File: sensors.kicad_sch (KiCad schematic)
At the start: 28 parts, among them J10 Conn_Coaxial, U3 LSM6DSOXTR, U4 LIS3MDL, U5 BNO055, U6 BME280, U7 ATGM336H-5N31, Y3 32.768KHz 12.5pF

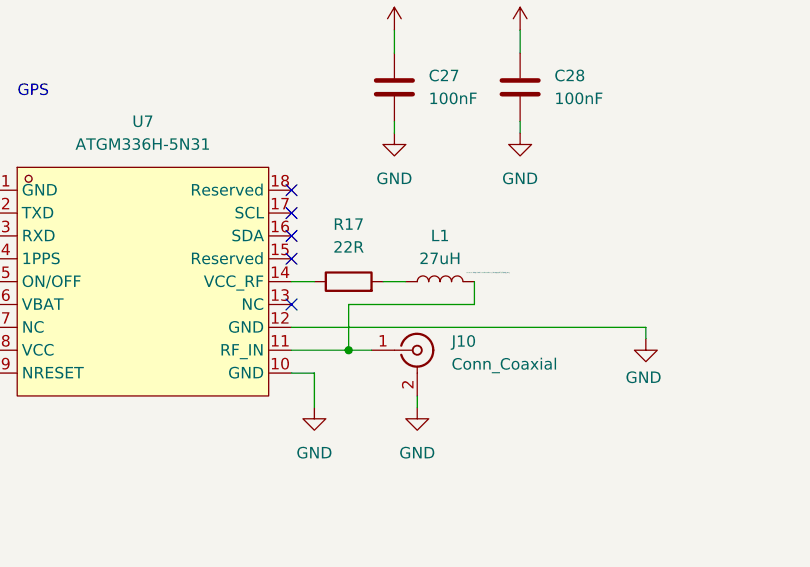
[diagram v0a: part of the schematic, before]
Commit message: GPS Bias tee upgrade
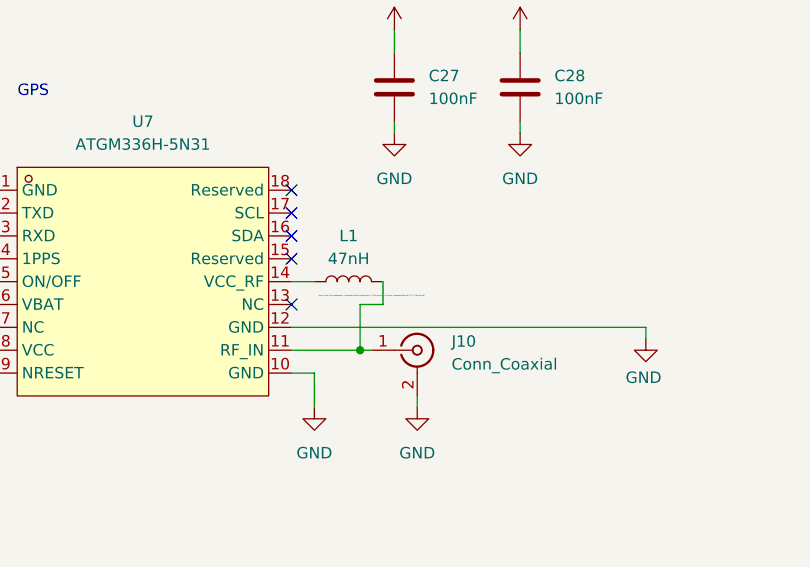
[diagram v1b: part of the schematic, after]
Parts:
- removed R17: 22R, symbol Device:R
- L1: value 27uH -> 47nH
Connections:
- net at U7.14 (VCC_RF): now also L1.1
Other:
- note added: "source: http://wiki.sunfounder.cc/images/f/f1/Gsdg.png and page 13 of https://www.tinytronics.nl/product_files/002176_ATGM336H.pdf"
- note removed: "source: http://wiki.sunfounder.cc/images/f/f1/Gsdg.png"
- moved on the sheet: L1
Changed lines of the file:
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@@
 		)
 	)
-	(text "source: http://wiki.sunfounder.cc/images/f/f1/Gsdg.png"
+	(text "source: http://wiki.sunfounder.cc/images/f/f1/Gsdg.png and page 13 of https://www.tinytronics.nl/product_files/002176_ATGM336H.pdf"
 		(exclude_from_sim no)
-		(at 171.704 149.098 0)
+		(at 158.75 151.638 0)
 		(effects
 			(font
@@
 	)
 	(junction
-		(at 156.21 157.48)
-		(diameter 0)
-		(color 0 0 0 0)
-	)
-	(junction
 		(at 175.26 52.07)
 		(diameter 0)
@@
 		(color 0 0 0 0)
 	)
+	(junction
+		(at 157.48 157.48)
+		(diameter 0)
+		(color 0 0 0 0)
+	)
 	(no_connect
 		(at 116.84 154.94)
@@
 	(wire
 		(pts
-			(xy 170.18 149.86) (xy 170.18 152.4)
+			(xy 157.48 152.4) (xy 157.48 157.48)
 		)
 		(stroke
@@
 	(wire
 		(pts
-			(xy 160.02 149.86) (xy 162.56 149.86)
+			(xy 114.3 157.48) (xy 116.84 157.48)
 		)
 		(stroke
@@
 	(wire
 		(pts
-			(xy 114.3 157.48) (xy 116.84 157.48)
+			(xy 53.34 66.04) (xy 67.31 66.04)
 		)
 		(stroke
@@
 	(wire
 		(pts
-			(xy 53.34 66.04) (xy 67.31 66.04)
+			(xy 91.44 158.75) (xy 113.03 158.75)
 		)
 		(stroke
@@
 	(wire
 		(pts
-			(xy 91.44 158.75) (xy 113.03 158.75)
+			(xy 152.4 149.86) (xy 149.86 149.86)
 		)
 		(stroke
@@
 	(wire
 		(pts
-			(xy 156.21 157.48) (xy 158.75 157.48)
-		)
-		(stroke
-			(width 0)
-			(type default)
-		)
-	)
-	(wire
-		(pts
 			(xy 95.25 140.97) (xy 95.25 138.43)
 		)
@@
 	(wire
 		(pts
-			(xy 189.23 156.21) (xy 189.23 154.94)
+			(xy 160.02 152.4) (xy 160.02 149.86)
 		)
 		(stroke
@@
 	(wire
 		(pts
-			(xy 99.06 91.44) (xy 99.06 93.98)
+			(xy 189.23 156.21) (xy 189.23 154.94)
 		)
 		(stroke
@@
 	(wire
 		(pts
-			(xy 181.61 46.99) (xy 175.26 46.99)
+			(xy 99.06 91.44) (xy 99.06 93.98)
 		)
 		(stroke
@@
 	(wire
 		(pts
-			(xy 233.68 39.37) (xy 233.68 36.83)
+			(xy 181.61 46.99) (xy 175.26 46.99)
 		)
 		(stroke
@@
 	(wire
 		(pts
-			(xy 257.81 92.71) (xy 260.35 92.71)
+			(xy 233.68 39.37) (xy 233.68 36.83)
 		)
 		(stroke
@@
 	(wire
 		(pts
-			(xy 170.18 152.4) (xy 156.21 152.4)
+			(xy 257.81 92.71) (xy 260.35 92.71)
 		)
 		(stroke
@@
 	(wire
 		(pts
-			(xy 156.21 152.4) (xy 156.21 157.48)
-		)
-		(stroke
-			(width 0)
-			(type default)
-		)
-	)
-	(wire
-		(pts
 			(xy 101.6 143.51) (xy 101.6 140.97)
 		)
@@
 	(wire
 		(pts
-			(xy 149.86 157.48) (xy 156.21 157.48)
+			(xy 149.86 157.48) (xy 157.48 157.48)
 		)
 		(stroke
@@
 	(wire
 		(pts
+			(xy 157.48 157.48) (xy 158.75 157.48)
+		)
+		(stroke
+			(width 0)
+			(type default)
+		)
+	)
+	(wire
+		(pts
 			(xy 100.33 81.28) (xy 110.49 81.28)
 		)
@@
 	(wire
 		(pts
+			(xy 157.48 152.4) (xy 160.02 152.4)
+		)
+		(stroke
+			(width 0)
+			(type default)
+		)
+	)
+	(wire
+		(pts
 			(xy 116.84 83.82) (xy 111.76 83.82)
 		)
@@
 	(wire
 		(pts
-			(xy 149.86 149.86) (xy 152.4 149.86)
-		)
-		(stroke
-			(width 0)
-			(type default)
-		)
-	)
-	(wire
-		(pts
 			(xy 102.87 147.32) (xy 102.87 143.51)
 		)
@@
 	)
 	(symbol
-		(lib_id "Device:R")
-		(at 156.21 149.86 90)
-		(unit 1)
-		(exclude_from_sim no)
-		(in_bom yes)
-		(on_board yes)
-		(dnp no)
-		(fields_autoplaced yes)
-		(property "Reference" "R17"
-			(at 156.21 143.51 90)
-			(effects
-				(font
-					(size 1.27 1.27)
-				)
-			)
-		)
-		(property "Value" "22R"
-			(at 156.21 146.05 90)
-			(effects
-				(font
-					(size 1.27 1.27)
-				)
-			)
-		)
-		(property "Footprint" ""
-			(at 156.21 151.638 90)
-			(effects
-				(font
-					(size 1.27 1.27)
-				)
-				(hide yes)
-			)
-		)
-		(property "Datasheet" "~"
-			(at 156.21 149.86 0)
-			(effects
-				(font
-					(size 1.27 1.27)
-				)
-				(hide yes)
-			)
-		)
-		(property "Description" "Resistor"
-			(at 156.21 149.86 0)
-			(effects
-				(font
-					(size 1.27 1.27)
-				)
-				(hide yes)
-			)
-		)
-		(pin "1"
-		)
-		(pin "2"
-		)
-		(instances
-			(project ""
-				(path "/e99ca14d-cacc-4390-92ee-6dcff8e13ef3/ec279230-54a0-4e30-9b23-a4126e2291f2"
-					(reference "R17")
-					(unit 1)
-				)
-			)
-		)
-	)
-	(symbol
 		(lib_id "Device:C")
 		(at 111.76 54.61 90)
@@
 	(symbol
 		(lib_id "Device:L")
-		(at 166.37 149.86 90)
+		(at 156.21 149.86 90)
 		(unit 1)
 		(exclude_from_sim no)
@@
 		(on_board yes)
 		(dnp no)
-		(fields_autoplaced yes)
 		(property "Reference" "L1"
-			(at 166.37 144.78 90)
+			(at 156.21 144.78 90)
 			(effects
 				(font
@@
 			)
 		)
-		(property "Value" "27uH"
-			(at 166.37 147.32 90)
+		(property "Value" "47nH"
+			(at 156.21 147.32 90)
 			(effects
 				(font
@@
 		)
 		(property "Footprint" ""
-			(at 166.37 149.86 0)
+			(at 156.21 149.86 0)
 			(effects
 				(font
@@
 		)
 		(property "Datasheet" "~"
-			(at 166.37 149.86 0)
+			(at 156.21 149.86 0)
 			(effects
 				(font
@@
 		)
 		(property "Description" "Inductor"
-			(at 166.37 149.86 0)
+			(at 156.21 149.86 0)
 			(effects
 				(font

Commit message: Add more footprints!
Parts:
- C10, C11, C12, C13: footprint (none) -> Capacitor_SMD:C_0402_1005Metric_Pad0.74x0.62mm_HandSolder
- C14, C27, C28, C8, C9: footprint Capacitor_SMD:C_0603_1608Metric_Pad1.08x0.95mm_HandSolder -> Capacitor_SMD:C_0402_1005Metric_Pad0.74x0.62mm_HandSolder
- L1: footprint (none) -> Inductor_SMD:L_0603_1608Metric_Pad1.05x0.95mm_HandSolder
- R1, R19, R2, R3, R4, R7: footprint (none) -> Resistor_SMD:R_0402_1005Metric_Pad0.72x0.64mm_HandSolder
- R16, R18, R9: footprint Resistor_SMD:R_0603_1608Metric_Pad0.98x0.95mm_HandSolder -> Resistor_SMD:R_0402_1005Metric_Pad0.72x0.64mm_HandSolder
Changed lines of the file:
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@@
 			)
 		)
-		(property "Footprint" "Resistor_SMD:R_0603_1608Metric_Pad0.98x0.95mm_HandSolder"
+		(property "Footprint" "Resistor_SMD:R_0402_1005Metric_Pad0.72x0.64mm_HandSolder"
 			(at 59.69 164.592 90)
 			(effects
@@
 			)
 		)
-		(property "Footprint" ""
+		(property "Footprint" "Capacitor_SMD:C_0402_1005Metric_Pad0.74x0.62mm_HandSolder"
 			(at 257.81 91.7448 0)
 			(effects
@@
 			)
 		)
-		(property "Footprint" "Resistor_SMD:R_0603_1608Metric_Pad0.98x0.95mm_HandSolder"
+		(property "Footprint" "Resistor_SMD:R_0402_1005Metric_Pad0.72x0.64mm_HandSolder"
 			(at 62.23 152.908 90)
 			(effects
@@
 			)
 		)
-		(property "Footprint" "Capacitor_SMD:C_0603_1608Metric_Pad1.08x0.95mm_HandSolder"
+		(property "Footprint" "Capacitor_SMD:C_0402_1005Metric_Pad0.74x0.62mm_HandSolder"
 			(at 176.2252 132.08 0)
 			(effects
@@
 			)
 		)
-		(property "Footprint" "Capacitor_SMD:C_0603_1608Metric_Pad1.08x0.95mm_HandSolder"
+		(property "Footprint" "Capacitor_SMD:C_0402_1005Metric_Pad0.74x0.62mm_HandSolder"
 			(at 115.57 53.6448 0)
 			(effects
@@
 			)
 		)
-		(property "Footprint" "Capacitor_SMD:C_0603_1608Metric_Pad1.08x0.95mm_HandSolder"
+		(property "Footprint" "Capacitor_SMD:C_0402_1005Metric_Pad0.74x0.62mm_HandSolder"
 			(at 115.57 68.8848 0)
 			(effects
@@
 			)
 		)
-		(property "Footprint" ""
+		(property "Footprint" "Capacitor_SMD:C_0402_1005Metric_Pad0.74x0.62mm_HandSolder"
 			(at 189.23 46.0248 0)
 			(effects
@@
 			)
 		)
-		(property "Footprint" ""
+		(property "Footprint" "Resistor_SMD:R_0402_1005Metric_Pad0.72x0.64mm_HandSolder"
 			(at 231.902 33.02 90)
 			(effects
@@
 			)
 		)
-		(property "Footprint" ""
+		(property "Footprint" "Resistor_SMD:R_0402_1005Metric_Pad0.72x0.64mm_HandSolder"
 			(at 224.282 120.65 90)
 			(effects
@@
 			)
 		)
-		(property "Footprint" "Capacitor_SMD:C_0603_1608Metric_Pad1.08x0.95mm_HandSolder"
+		(property "Footprint" "Capacitor_SMD:C_0402_1005Metric_Pad0.74x0.62mm_HandSolder"
 			(at 162.2552 132.08 0)
 			(effects
@@
 			)
 		)
-		(property "Footprint" ""
+		(property "Footprint" "Capacitor_SMD:C_0402_1005Metric_Pad0.74x0.62mm_HandSolder"
 			(at 265.1252 121.92 0)
 			(effects
@@
 			)
 		)
-		(property "Footprint" ""
+		(property "Footprint" "Resistor_SMD:R_0402_1005Metric_Pad0.72x0.64mm_HandSolder"
 			(at 57.912 86.36 90)
 			(effects
@@
 			)
 		)
-		(property "Footprint" ""
+		(property "Footprint" "Resistor_SMD:R_0402_1005Metric_Pad0.72x0.64mm_HandSolder"
 			(at 60.452 50.8 90)
 			(effects
@@
 			)
 		)
-		(property "Footprint" "Capacitor_SMD:C_0603_1608Metric_Pad1.08x0.95mm_HandSolder"
+		(property "Footprint" "Capacitor_SMD:C_0402_1005Metric_Pad0.74x0.62mm_HandSolder"
 			(at 43.18 141.9352 0)
 			(effects
@@
 			)
 		)
-		(property "Footprint" ""
+		(property "Footprint" "Inductor_SMD:L_0603_1608Metric_Pad1.05x0.95mm_HandSolder"
 			(at 156.21 149.86 0)
 			(effects
@@
 			)
 		)
-		(property "Footprint" ""
+		(property "Footprint" "Capacitor_SMD:C_0402_1005Metric_Pad0.74x0.62mm_HandSolder"
 			(at 100.0252 91.44 0)
 			(effects
@@
 			)
 		)
-		(property "Footprint" ""
+		(property "Footprint" "Resistor_SMD:R_0402_1005Metric_Pad0.72x0.64mm_HandSolder"
 			(at 93.472 124.46 90)
 			(effects
@@
 			)
 		)
-		(property "Footprint" "Resistor_SMD:R_0603_1608Metric_Pad0.98x0.95mm_HandSolder"
+		(property "Footprint" "Resistor_SMD:R_0402_1005Metric_Pad0.72x0.64mm_HandSolder"
 			(at 99.06 151.638 90)
 			(effects
@@
 			)
 		)
-		(property "Footprint" ""
+		(property "Footprint" "Resistor_SMD:R_0402_1005Metric_Pad0.72x0.64mm_HandSolder"
 			(at 221.742 33.02 90)
 			(effects

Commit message: More schematic work
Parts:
- D1: footprint (none) -> LED_SMD:LED_0603_1608Metric
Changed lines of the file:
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@@
 			)
 		)
-		(property "Footprint" ""
+		(property "Footprint" "LED_SMD:LED_0603_1608Metric"
 			(at 95.25 134.62 0)
 			(effects

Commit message: Reset circuit fix (oops...)
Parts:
- removed C27, C28: 100nF, Capacitor_SMD:C_0402_1005Metric_Pad0.74x0.62mm_HandSolder, symbol Device:C
- added C31, C34, C38, C40, C41, C44: 100nF, Capacitor_SMD:C_0402_1005Metric_Pad0.74x0.62mm_HandSolder, symbol Device:C
- added C35, C39, C42, C45: 10uF, Capacitor_SMD:C_0402_1005Metric_Pad0.74x0.62mm_HandSolder, symbol Device:C
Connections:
- net +3.3V: now also C31.1, C34.1, C35.1, C38.1, C39.1, C40.1, C41.1, C42.1, C44.1, C45.1
- net GND: now also C31.2, C34.2, C35.2, C38.2, C39.2, C40.2, C41.2, C42.2, C44.2, C45.2
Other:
- note added: "Address = 0x1C"
- note added: "Address = 0x6A"
- title: (none) -> Guidance Sensors
- moved on the sheet: R2, R4

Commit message: Do a few reroutes
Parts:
- added C28: 10uF, Capacitor_SMD:C_0402_1005Metric_Pad0.74x0.62mm_HandSolder, symbol Device:C
- added R48: 10k, Resistor_SMD:R_0402_1005Metric_Pad0.72x0.64mm_HandSolder, symbol Device:R
- R2, R4: value 10k -> 2.2k
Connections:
- net +3.3V: now also C14.1, C28.1; no longer C14.2
- net GND: now also C14.2, C28.2, R48.2; no longer C14.1
- net at U3.1 (SDO/SA0): now also R48.1
- no-connect marks 13 -> 12
